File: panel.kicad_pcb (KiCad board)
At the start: 2 copper layers, 91.2 x 81.5 mm, 212 parts, among them J1 PinSocket_1x04_P2.54mm_Vertic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, U1 AP2112K-3.3

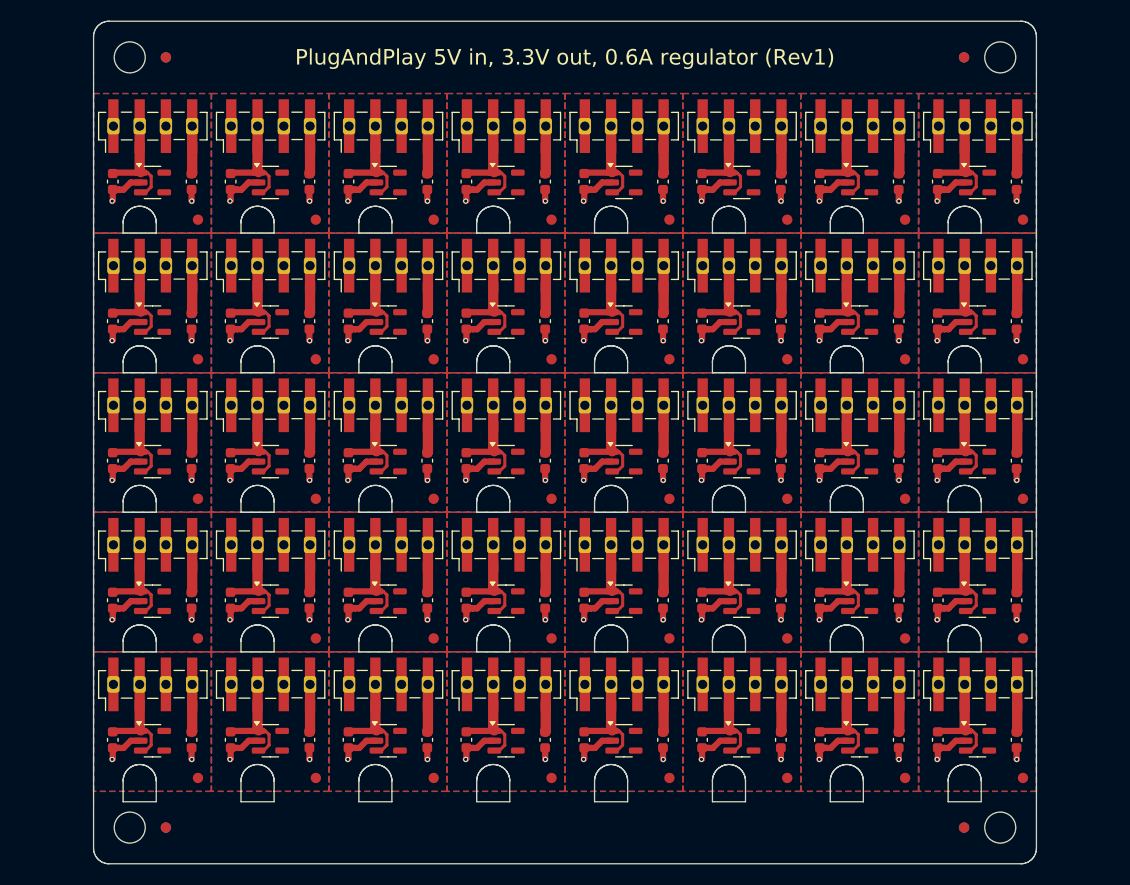
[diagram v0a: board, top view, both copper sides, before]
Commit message: Reduce the screw hole to match M2 screw
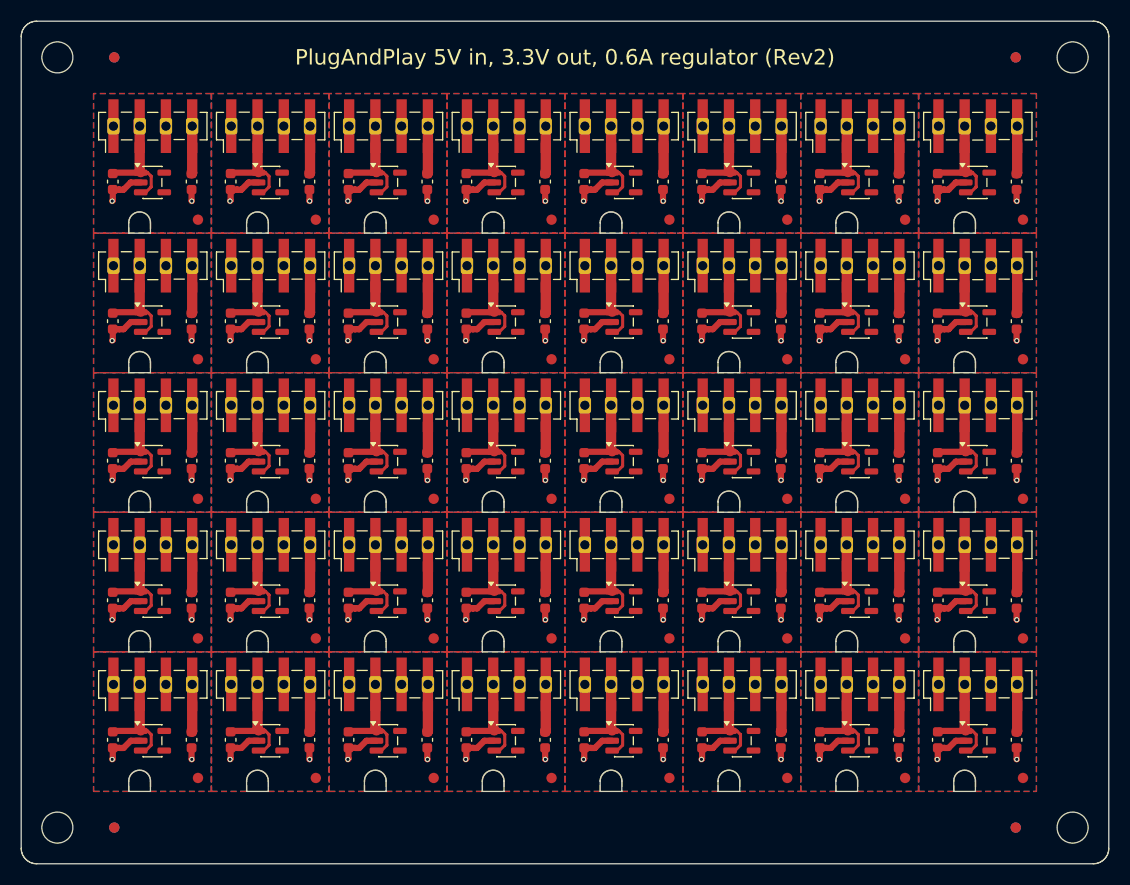
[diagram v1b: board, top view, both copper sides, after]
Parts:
- removed the C1 at (61.3, 76.0)
- removed the C1 at (118.3, 49.0)
- removed the C1 at (141.1, 62.5)
- removed the C1 at (118.3, 35.5)
- removed the C1 at (129.7, 89.5)
- removed the C1 at (84.1, 49.0)
- removed the C1 at (129.7, 49.0)
- removed the C1 at (84.1, 76.0)
- removed the C1 at (84.1, 89.5)
- removed the C1 at (141.1, 49.0)
- removed the C1 at (84.1, 62.5)
- removed the C1 at (95.5, 35.5)
- removed the C1 at (118.3, 62.5)
- removed the C1 at (61.3, 89.5)
- removed the C1 at (72.7, 76.0)
- removed the C1 at (95.5, 76.0)
- removed the C1 at (72.7, 62.5)
- removed the C1 at (118.3, 76.0)
- removed the C1 at (106.9, 49.0)
- removed the C1 at (84.1, 35.5)
- removed the C1 at (106.9, 76.0)
- removed the C1 at (129.7, 76.0)
- removed the C1 at (106.9, 62.5)
- removed the C1 at (72.7, 35.5)
- removed the C1 at (129.7, 62.5)
- removed the C1 at (61.3, 49.0)
- removed the C1 at (118.3, 89.5)
- removed the C1 at (95.5, 62.5)
- removed the C1 at (141.1, 89.5)
- removed the C1 at (72.7, 89.5)
- removed the C1 at (61.3, 35.5)
- removed the C1 at (141.1, 35.5)
- removed the C1 at (61.3, 62.5)
- removed the C1 at (95.5, 49.0)
- removed the C1 at (141.1, 76.0)
- removed the C1 at (129.7, 35.5)
- removed the C1 at (72.7, 49.0)
- removed the C1 at (106.9, 89.5)
- removed the C1 at (106.9, 35.5)
- removed the C1 at (95.5, 89.5)
- removed the C2 at (125.9, 35.5)
- removed the C2 at (137.3, 76.0)
- removed the C2 at (91.7, 35.5)
- removed the C2 at (80.3, 89.5)
- removed the C2 at (68.9, 35.5)
- removed the C2 at (137.3, 62.5)
- removed the C2 at (91.7, 49.0)
- removed the C2 at (114.5, 76.0)
- removed the C2 at (114.5, 89.5)
- removed the C2 at (125.9, 62.5)
- removed the C2 at (103.1, 89.5)
- removed the C2 at (125.9, 49.0)
- removed the C2 at (137.3, 35.5)
- removed the C2 at (68.9, 62.5)
- removed the C2 at (148.7, 49.0)
- removed the C2 at (91.7, 76.0)
- removed the C2 at (137.3, 89.5)
- removed the C2 at (68.9, 49.0)
- removed the C2 at (125.9, 76.0)
- removed the C2 at (68.9, 76.0)
- removed the C2 at (148.7, 35.5)
- removed the C2 at (68.9, 89.5)
- removed the C2 at (80.3, 49.0)
- removed the C2 at (103.1, 49.0)
- removed the C2 at (137.3, 49.0)
- removed the C2 at (148.7, 89.5)
- removed the C2 at (80.3, 62.5)
- removed the C2 at (91.7, 62.5)
- removed the C2 at (103.1, 76.0)
- removed the C2 at (114.5, 49.0)
- removed the C2 at (114.5, 35.5)
- removed the C2 at (103.1, 62.5)
- removed the C2 at (148.7, 62.5)
- removed the C2 at (80.3, 35.5)
- removed the C2 at (114.5, 62.5)
- removed the C2 at (91.7, 89.5)
- removed the C2 at (125.9, 89.5)
- removed the C2 at (148.7, 76.0)
- removed the C2 at (103.1, 35.5)
- removed the C2 at (80.3, 76.0)
- removed the J1 at (133.5, 84.1)
- removed the J1 at (133.5, 57.1)
- removed the J1 at (87.9, 30.1)
- removed the J1 at (99.3, 43.6)
- removed the J1 at (133.5, 70.6)
- removed the J1 at (87.9, 43.6)
- removed the J1 at (76.5, 30.1)
- removed the J1 at (133.5, 30.1)
- removed the J1 at (76.5, 57.1)
- removed the J1 at (87.9, 84.1)
- removed the J1 at (87.9, 57.1)
- removed the J1 at (122.1, 70.6)
- removed the J1 at (122.1, 57.1)
- removed the J1 at (144.9, 57.1)
- removed the J1 at (65.1, 84.1)
- removed the J1 at (133.5, 43.6)
- removed the J1 at (144.9, 43.6)
- removed the J1 at (110.7, 30.1)
- removed the J1 at (144.9, 30.1)
- removed the J1 at (65.1, 43.6)
- removed the J1 at (122.1, 84.1)
- removed the J1 at (122.1, 43.6)
- removed the J1 at (110.7, 70.6)
- removed the J1 at (87.9, 70.6)
- removed the J1 at (110.7, 57.1)
- removed the J1 at (65.1, 30.1)
- removed the J1 at (122.1, 30.1)
- removed the J1 at (99.3, 57.1)
- removed the J1 at (110.7, 84.1)
- removed the J1 at (65.1, 70.6)
- removed the J1 at (99.3, 30.1)
- removed the J1 at (76.5, 43.6)
- removed the J1 at (65.1, 57.1)
- removed the J1 at (99.3, 84.1)
- removed the J1 at (110.7, 43.6)
- removed the J1 at (76.5, 84.1)
- removed the J1 at (99.3, 70.6)
- removed the J1 at (144.9, 70.6)
- removed the J1 at (76.5, 70.6)
- removed the J1 at (144.9, 84.1)
- removed the REF** at (69.5, 52.7)
- removed the REF** at (69.5, 66.2)
- removed the REF** at (126.5, 52.7)
- removed the REF** at (69.5, 39.2)
- removed the REF** at (149.3, 66.2)
- removed the REF** at (80.9, 79.7)
- removed the REF** at (137.9, 66.2)
- removed the REF** at (115.1, 79.7)
- removed the REF** at (137.9, 52.7)
- removed the REF** at (149.3, 39.2)
- removed the REF** at (92.3, 52.7)
- removed the REF** at (137.9, 93.2)
- removed the REF** at (115.1, 39.2)
- removed the REF** at (115.1, 66.2)
- removed the REF** at (92.3, 39.2)
- removed the REF** at (126.5, 79.7)
- removed the REF** at (80.9, 93.2)
- removed the REF** at (69.5, 93.2)
- removed the REF** at (80.9, 66.2)
- removed the REF** at (92.3, 66.2)
- removed the REF** at (149.3, 52.7)
- removed the REF** at (149.3, 79.7)
- removed the REF** at (115.1, 52.7)
- removed the REF** at (115.1, 93.2)
- removed the REF** at (103.7, 52.7)
- removed the REF** at (103.7, 39.2)
- removed the REF** at (137.9, 39.2)
- removed the REF** at (126.5, 93.2)
- removed the REF** at (137.9, 79.7)
- removed the REF** at (92.3, 93.2)
- removed the REF** at (103.7, 66.2)
- removed the REF** at (126.5, 39.2)
- removed the REF** at (92.3, 79.7)
- removed the REF** at (69.5, 79.7)
- removed the REF** at (126.5, 66.2)
- removed the REF** at (149.3, 93.2)
- removed the REF** at (103.7, 79.7)
- removed the REF** at (80.9, 39.2)
- removed the REF** at (80.9, 52.7)
- removed the REF** at (103.7, 93.2)
- removed the U1 at (87.9, 35.6)
- removed the U1 at (65.1, 76.1)
- removed the U1 at (99.3, 89.6)
- removed the U1 at (144.9, 49.1)
- removed the U1 at (133.5, 76.1)
- removed the U1 at (99.3, 49.1)
- removed the U1 at (110.7, 35.6)
- removed the U1 at (122.1, 35.6)
- removed the U1 at (110.7, 89.6)
- removed the U1 at (76.5, 62.6)
- removed the U1 at (87.9, 49.1)
- removed the U1 at (144.9, 35.6)
- removed the U1 at (133.5, 62.6)
- removed the U1 at (110.7, 76.1)
- removed the U1 at (76.5, 35.6)
- removed the U1 at (122.1, 49.1)
- removed the U1 at (133.5, 49.1)
- removed the U1 at (144.9, 89.6)
- removed the U1 at (99.3, 35.6)
- removed the U1 at (76.5, 76.1)
- removed the U1 at (65.1, 89.6)
- removed the U1 at (76.5, 49.1)
- removed the U1 at (65.1, 62.6)
- removed the U1 at (122.1, 76.1)
- removed the U1 at (65.1, 49.1)
- removed the U1 at (65.1, 35.6)
- removed the U1 at (144.9, 76.1)
- removed the U1 at (122.1, 62.6)
- removed the U1 at (99.3, 76.1)
- removed the U1 at (110.7, 49.1)
- removed the U1 at (122.1, 89.6)
- removed the U1 at (87.9, 62.6)
- removed the U1 at (133.5, 89.6)
- removed the U1 at (87.9, 76.1)
- removed the U1 at (110.7, 62.6)
- removed the U1 at (76.5, 89.6)
- removed the U1 at (133.5, 35.6)
- removed the U1 at (99.3, 62.6)
- removed the U1 at (87.9, 89.6)
- removed the U1 at (144.9, 62.6)
- added C1: 1uF, Capacitor_SMD:C_0603_1608Metric, F.Cu at (118.3, 49.0)
- added C1: 1uF, Capacitor_SMD:C_0603_1608Metric, F.Cu at (106.9, 76.0)
- added C1: 1uF, Capacitor_SMD:C_0603_1608Metric, F.Cu at (95.5, 62.5)
- added C1: 1uF, Capacitor_SMD:C_0603_1608Metric, F.Cu at (129.7, 49.0)
- added C1: 1uF, Capacitor_SMD:C_0603_1608Metric, F.Cu at (129.7, 76.0)
- added C1: 1uF, Capacitor_SMD:C_0603_1608Metric, F.Cu at (118.3, 89.5)
- added C1: 1uF, Capacitor_SMD:C_0603_1608Metric, F.Cu at (141.1, 35.5)
- added C1: 1uF, Capacitor_SMD:C_0603_1608Metric, F.Cu at (72.7, 49.0)
- added C1: 1uF, Capacitor_SMD:C_0603_1608Metric, F.Cu at (84.1, 35.5)
- added C1: 1uF, Capacitor_SMD:C_0603_1608Metric, F.Cu at (95.5, 35.5)
- added C1: 1uF, Capacitor_SMD:C_0603_1608Metric, F.Cu at (129.7, 89.5)
- added C1: 1uF, Capacitor_SMD:C_0603_1608Metric, F.Cu at (84.1, 62.5)
- added C1: 1uF, Capacitor_SMD:C_0603_1608Metric, F.Cu at (72.7, 89.5)
- added C1: 1uF, Capacitor_SMD:C_0603_1608Metric, F.Cu at (95.5, 49.0)
- added C1: 1uF, Capacitor_SMD:C_0603_1608Metric, F.Cu at (141.1, 76.0)
- added C1: 1uF, Capacitor_SMD:C_0603_1608Metric, F.Cu at (141.1, 89.5)
- added C1: 1uF, Capacitor_SMD:C_0603_1608Metric, F.Cu at (106.9, 49.0)
- added C1: 1uF, Capacitor_SMD:C_0603_1608Metric, F.Cu at (129.7, 35.5)
- added C1: 1uF, Capacitor_SMD:C_0603_1608Metric, F.Cu at (95.5, 89.5)
- added C1: 1uF, Capacitor_SMD:C_0603_1608Metric, F.Cu at (84.1, 76.0)
- added C1: 1uF, Capacitor_SMD:C_0603_1608Metric, F.Cu at (118.3, 62.5)
- added C1: 1uF, Capacitor_SMD:C_0603_1608Metric, F.Cu at (84.1, 49.0)
- added C1: 1uF, Capacitor_SMD:C_0603_1608Metric, F.Cu at (141.1, 49.0)
- added C1: 1uF, Capacitor_SMD:C_0603_1608Metric, F.Cu at (61.3, 49.0)
- added C1: 1uF, Capacitor_SMD:C_0603_1608Metric, F.Cu at (141.1, 62.5)
- added C1: 1uF, Capacitor_SMD:C_0603_1608Metric, F.Cu at (84.1, 89.5)
- added C1: 1uF, Capacitor_SMD:C_0603_1608Metric, F.Cu at (72.7, 35.5)
- added C1: 1uF, Capacitor_SMD:C_0603_1608Metric, F.Cu at (95.5, 76.0)
- added C1: 1uF, Capacitor_SMD:C_0603_1608Metric, F.Cu at (106.9, 89.5)
- added C1: 1uF, Capacitor_SMD:C_0603_1608Metric, F.Cu at (72.7, 62.5)
- added C1: 1uF, Capacitor_SMD:C_0603_1608Metric, F.Cu at (72.7, 76.0)
- added C1: 1uF, Capacitor_SMD:C_0603_1608Metric, F.Cu at (61.3, 35.5)
- added C1: 1uF, Capacitor_SMD:C_0603_1608Metric, F.Cu at (129.7, 62.5)
- added C1: 1uF, Capacitor_SMD:C_0603_1608Metric, F.Cu at (61.3, 62.5)
- added C1: 1uF, Capacitor_SMD:C_0603_1608Metric, F.Cu at (118.3, 76.0)
- added C1: 1uF, Capacitor_SMD:C_0603_1608Metric, F.Cu at (61.3, 89.5)
- added C1: 1uF, Capacitor_SMD:C_0603_1608Metric, F.Cu at (61.3, 76.0)
- added C1: 1uF, Capacitor_SMD:C_0603_1608Metric, F.Cu at (106.9, 62.5)
- added C1: 1uF, Capacitor_SMD:C_0603_1608Metric, F.Cu at (106.9, 35.5)
- added C1: 1uF, Capacitor_SMD:C_0603_1608Metric, F.Cu at (118.3, 35.5)
- added C2: 1uF, Capacitor_SMD:C_0603_1608Metric, F.Cu at (91.7, 76.0)
- added C2: 1uF, Capacitor_SMD:C_0603_1608Metric, F.Cu at (148.7, 35.5)
- added C2: 1uF, Capacitor_SMD:C_0603_1608Metric, F.Cu at (137.3, 89.5)
- added C2: 1uF, Capacitor_SMD:C_0603_1608Metric, F.Cu at (91.7, 89.5)
- added C2: 1uF, Capacitor_SMD:C_0603_1608Metric, F.Cu at (103.1, 89.5)
- added C2: 1uF, Capacitor_SMD:C_0603_1608Metric, F.Cu at (80.3, 35.5)
- added C2: 1uF, Capacitor_SMD:C_0603_1608Metric, F.Cu at (148.7, 89.5)
- added C2: 1uF, Capacitor_SMD:C_0603_1608Metric, F.Cu at (80.3, 62.5)
- added C2: 1uF, Capacitor_SMD:C_0603_1608Metric, F.Cu at (125.9, 89.5)
- added C2: 1uF, Capacitor_SMD:C_0603_1608Metric, F.Cu at (103.1, 49.0)
- added C2: 1uF, Capacitor_SMD:C_0603_1608Metric, F.Cu at (68.9, 49.0)
- added C2: 1uF, Capacitor_SMD:C_0603_1608Metric, F.Cu at (91.7, 49.0)
- added C2: 1uF, Capacitor_SMD:C_0603_1608Metric, F.Cu at (148.7, 76.0)
- added C2: 1uF, Capacitor_SMD:C_0603_1608Metric, F.Cu at (103.1, 76.0)
- added C2: 1uF, Capacitor_SMD:C_0603_1608Metric, F.Cu at (148.7, 62.5)
- added C2: 1uF, Capacitor_SMD:C_0603_1608Metric, F.Cu at (137.3, 62.5)
- added C2: 1uF, Capacitor_SMD:C_0603_1608Metric, F.Cu at (91.7, 35.5)
- added C2: 1uF, Capacitor_SMD:C_0603_1608Metric, F.Cu at (148.7, 49.0)
- added C2: 1uF, Capacitor_SMD:C_0603_1608Metric, F.Cu at (114.5, 89.5)
- added C2: 1uF, Capacitor_SMD:C_0603_1608Metric, F.Cu at (114.5, 49.0)
- added C2: 1uF, Capacitor_SMD:C_0603_1608Metric, F.Cu at (103.1, 35.5)
- added C2: 1uF, Capacitor_SMD:C_0603_1608Metric, F.Cu at (68.9, 76.0)
- added C2: 1uF, Capacitor_SMD:C_0603_1608Metric, F.Cu at (68.9, 35.5)
- added C2: 1uF, Capacitor_SMD:C_0603_1608Metric, F.Cu at (114.5, 35.5)
- added C2: 1uF, Capacitor_SMD:C_0603_1608Metric, F.Cu at (114.5, 62.5)
- added C2: 1uF, Capacitor_SMD:C_0603_1608Metric, F.Cu at (80.3, 89.5)
- added C2: 1uF, Capacitor_SMD:C_0603_1608Metric, F.Cu at (125.9, 49.0)
- added C2: 1uF, Capacitor_SMD:C_0603_1608Metric, F.Cu at (68.9, 89.5)
- added C2: 1uF, Capacitor_SMD:C_0603_1608Metric, F.Cu at (137.3, 35.5)
- added C2: 1uF, Capacitor_SMD:C_0603_1608Metric, F.Cu at (103.1, 62.5)
- added C2: 1uF, Capacitor_SMD:C_0603_1608Metric, F.Cu at (125.9, 76.0)
- added C2: 1uF, Capacitor_SMD:C_0603_1608Metric, F.Cu at (137.3, 76.0)
- added C2: 1uF, Capacitor_SMD:C_0603_1608Metric, F.Cu at (125.9, 62.5)
- added C2: 1uF, Capacitor_SMD:C_0603_1608Metric, F.Cu at (125.9, 35.5)
- added C2: 1uF, Capacitor_SMD:C_0603_1608Metric, F.Cu at (80.3, 49.0)
- added C2: 1uF, Capacitor_SMD:C_0603_1608Metric, F.Cu at (137.3, 49.0)
- added C2: 1uF, Capacitor_SMD:C_0603_1608Metric, F.Cu at (114.5, 76.0)
- added C2: 1uF, Capacitor_SMD:C_0603_1608Metric, F.Cu at (80.3, 76.0)
- added C2: 1uF, Capacitor_SMD:C_0603_1608Metric, F.Cu at (68.9, 62.5)
- added C2: 1uF, Capacitor_SMD:C_0603_1608Metric, F.Cu at (91.7, 62.5)
- added J1: PinSocket_1x04_P2.54mm_Vertical_SMD_Pin1Left, Library:PinSocket_1x04_P2.54mm_Vertical_SMD_Pin1Left, F.Cu at (87.9, 70.7)
- added J1: PinSocket_1x04_P2.54mm_Vertical_SMD_Pin1Left, Library:PinSocket_1x04_P2.54mm_Vertical_SMD_Pin1Left, F.Cu at (122.1, 43.6)
- added J1: PinSocket_1x04_P2.54mm_Vertical_SMD_Pin1Left, Library:PinSocket_1x04_P2.54mm_Vertical_SMD_Pin1Left, F.Cu at (133.5, 43.6)
- added J1: PinSocket_1x04_P2.54mm_Vertical_SMD_Pin1Left, Library:PinSocket_1x04_P2.54mm_Vertical_SMD_Pin1Left, F.Cu at (122.1, 57.1)
- added J1: PinSocket_1x04_P2.54mm_Vertical_SMD_Pin1Left, Library:PinSocket_1x04_P2.54mm_Vertical_SMD_Pin1Left, F.Cu at (122.1, 30.1)
- added J1: PinSocket_1x04_P2.54mm_Vertical_SMD_Pin1Left, Library:PinSocket_1x04_P2.54mm_Vertical_SMD_Pin1Left, F.Cu at (76.5, 30.1)
- added J1: PinSocket_1x04_P2.54mm_Vertical_SMD_Pin1Left, Library:PinSocket_1x04_P2.54mm_Vertical_SMD_Pin1Left, F.Cu at (99.3, 57.1)
- added J1: PinSocket_1x04_P2.54mm_Vertical_SMD_Pin1Left, Library:PinSocket_1x04_P2.54mm_Vertical_SMD_Pin1Left, F.Cu at (133.5, 57.1)
- added J1: PinSocket_1x04_P2.54mm_Vertical_SMD_Pin1Left, Library:PinSocket_1x04_P2.54mm_Vertical_SMD_Pin1Left, F.Cu at (99.3, 43.6)
- added J1: PinSocket_1x04_P2.54mm_Vertical_SMD_Pin1Left, Library:PinSocket_1x04_P2.54mm_Vertical_SMD_Pin1Left, F.Cu at (144.9, 57.1)
- added J1: PinSocket_1x04_P2.54mm_Vertical_SMD_Pin1Left, Library:PinSocket_1x04_P2.54mm_Vertical_SMD_Pin1Left, F.Cu at (65.1, 57.1)
- added J1: PinSocket_1x04_P2.54mm_Vertical_SMD_Pin1Left, Library:PinSocket_1x04_P2.54mm_Vertical_SMD_Pin1Left, F.Cu at (144.9, 30.1)
- added J1: PinSocket_1x04_P2.54mm_Vertical_SMD_Pin1Left, Library:PinSocket_1x04_P2.54mm_Vertical_SMD_Pin1Left, F.Cu at (144.9, 43.6)
- added J1: PinSocket_1x04_P2.54mm_Vertical_SMD_Pin1Left, Library:PinSocket_1x04_P2.54mm_Vertical_SMD_Pin1Left, F.Cu at (133.5, 84.2)
- added J1: PinSocket_1x04_P2.54mm_Vertical_SMD_Pin1Left, Library:PinSocket_1x04_P2.54mm_Vertical_SMD_Pin1Left, F.Cu at (76.5, 43.6)
- added J1: PinSocket_1x04_P2.54mm_Vertical_SMD_Pin1Left, Library:PinSocket_1x04_P2.54mm_Vertical_SMD_Pin1Left, F.Cu at (110.7, 70.7)
- added J1: PinSocket_1x04_P2.54mm_Vertical_SMD_Pin1Left, Library:PinSocket_1x04_P2.54mm_Vertical_SMD_Pin1Left, F.Cu at (87.9, 57.1)
- added J1: PinSocket_1x04_P2.54mm_Vertical_SMD_Pin1Left, Library:PinSocket_1x04_P2.54mm_Vertical_SMD_Pin1Left, F.Cu at (76.5, 70.7)
- added J1: PinSocket_1x04_P2.54mm_Vertical_SMD_Pin1Left, Library:PinSocket_1x04_P2.54mm_Vertical_SMD_Pin1Left, F.Cu at (110.7, 30.1)
- added J1: PinSocket_1x04_P2.54mm_Vertical_SMD_Pin1Left, Library:PinSocket_1x04_P2.54mm_Vertical_SMD_Pin1Left, F.Cu at (133.5, 30.1)
- added J1: PinSocket_1x04_P2.54mm_Vertical_SMD_Pin1Left, Library:PinSocket_1x04_P2.54mm_Vertical_SMD_Pin1Left, F.Cu at (99.3, 30.1)
- added J1: PinSocket_1x04_P2.54mm_Vertical_SMD_Pin1Left, Library:PinSocket_1x04_P2.54mm_Vertical_SMD_Pin1Left, F.Cu at (87.9, 84.2)
- added J1: PinSocket_1x04_P2.54mm_Vertical_SMD_Pin1Left, Library:PinSocket_1x04_P2.54mm_Vertical_SMD_Pin1Left, F.Cu at (65.1, 43.6)
- added J1: PinSocket_1x04_P2.54mm_Vertical_SMD_Pin1Left, Library:PinSocket_1x04_P2.54mm_Vertical_SMD_Pin1Left, F.Cu at (122.1, 84.2)
- added J1: PinSocket_1x04_P2.54mm_Vertical_SMD_Pin1Left, Library:PinSocket_1x04_P2.54mm_Vertical_SMD_Pin1Left, F.Cu at (144.9, 84.2)
- added J1: PinSocket_1x04_P2.54mm_Vertical_SMD_Pin1Left, Library:PinSocket_1x04_P2.54mm_Vertical_SMD_Pin1Left, F.Cu at (110.7, 43.6)
- added J1: PinSocket_1x04_P2.54mm_Vertical_SMD_Pin1Left, Library:PinSocket_1x04_P2.54mm_Vertical_SMD_Pin1Left, F.Cu at (122.1, 70.7)
- added J1: PinSocket_1x04_P2.54mm_Vertical_SMD_Pin1Left, Library:PinSocket_1x04_P2.54mm_Vertical_SMD_Pin1Left, F.Cu at (144.9, 70.7)
- added J1: PinSocket_1x04_P2.54mm_Vertical_SMD_Pin1Left, Library:PinSocket_1x04_P2.54mm_Vertical_SMD_Pin1Left, F.Cu at (76.5, 57.1)
- added J1: PinSocket_1x04_P2.54mm_Vertical_SMD_Pin1Left, Library:PinSocket_1x04_P2.54mm_Vertical_SMD_Pin1Left, F.Cu at (65.1, 30.1)
- added J1: PinSocket_1x04_P2.54mm_Vertical_SMD_Pin1Left, Library:PinSocket_1x04_P2.54mm_Vertical_SMD_Pin1Left, F.Cu at (65.1, 84.2)
- added J1: PinSocket_1x04_P2.54mm_Vertical_SMD_Pin1Left, Library:PinSocket_1x04_P2.54mm_Vertical_SMD_Pin1Left, F.Cu at (65.1, 70.7)
- added J1: PinSocket_1x04_P2.54mm_Vertical_SMD_Pin1Left, Library:PinSocket_1x04_P2.54mm_Vertical_SMD_Pin1Left, F.Cu at (133.5, 70.7)
- added J1: PinSocket_1x04_P2.54mm_Vertical_SMD_Pin1Left, Library:PinSocket_1x04_P2.54mm_Vertical_SMD_Pin1Left, F.Cu at (110.7, 57.1)
- added J1: PinSocket_1x04_P2.54mm_Vertical_SMD_Pin1Left, Library:PinSocket_1x04_P2.54mm_Vertical_SMD_Pin1Left, F.Cu at (87.9, 43.6)
- added J1: PinSocket_1x04_P2.54mm_Vertical_SMD_Pin1Left, Library:PinSocket_1x04_P2.54mm_Vertical_SMD_Pin1Left, F.Cu at (76.5, 84.2)
- added J1: PinSocket_1x04_P2.54mm_Vertical_SMD_Pin1Left, Library:PinSocket_1x04_P2.54mm_Vertical_SMD_Pin1Left, F.Cu at (87.9, 30.1)
- added J1: PinSocket_1x04_P2.54mm_Vertical_SMD_Pin1Left, Library:PinSocket_1x04_P2.54mm_Vertical_SMD_Pin1Left, F.Cu at (99.3, 84.2)
- added J1: PinSocket_1x04_P2.54mm_Vertical_SMD_Pin1Left, Library:PinSocket_1x04_P2.54mm_Vertical_SMD_Pin1Left, F.Cu at (99.3, 70.7)
- added J1: PinSocket_1x04_P2.54mm_Vertical_SMD_Pin1Left, Library:PinSocket_1x04_P2.54mm_Vertical_SMD_Pin1Left, F.Cu at (110.7, 84.2)
- added REF**: Fiducial_1mm_Mask2mm, Fiducial:Fiducial_1mm_Mask2mm, F.Cu at (103.7, 66.2)
- added REF**: Fiducial_1mm_Mask2mm, Fiducial:Fiducial_1mm_Mask2mm, F.Cu at (115.1, 39.2)
- added REF**: Fiducial_1mm_Mask2mm, Fiducial:Fiducial_1mm_Mask2mm, F.Cu at (69.5, 39.2)
- added REF**: Fiducial_1mm_Mask2mm, Fiducial:Fiducial_1mm_Mask2mm, F.Cu at (69.5, 52.7)
- added REF**: Fiducial_1mm_Mask2mm, Fiducial:Fiducial_1mm_Mask2mm, F.Cu at (137.9, 79.7)
- added REF**: Fiducial_1mm_Mask2mm, Fiducial:Fiducial_1mm_Mask2mm, F.Cu at (69.5, 93.2)
- added REF**: Fiducial_1mm_Mask2mm, Fiducial:Fiducial_1mm_Mask2mm, F.Cu at (103.7, 79.7)
- added REF**: Fiducial_1mm_Mask2mm, Fiducial:Fiducial_1mm_Mask2mm, F.Cu at (126.5, 79.7)
- added REF**: Fiducial_1mm_Mask2mm, Fiducial:Fiducial_1mm_Mask2mm, F.Cu at (115.1, 52.7)
- added REF**: Fiducial_1mm_Mask2mm, Fiducial:Fiducial_1mm_Mask2mm, F.Cu at (115.1, 79.7)
- added REF**: Fiducial_1mm_Mask2mm, Fiducial:Fiducial_1mm_Mask2mm, F.Cu at (69.5, 79.7)
- added REF**: Fiducial_1mm_Mask2mm, Fiducial:Fiducial_1mm_Mask2mm, F.Cu at (80.9, 39.2)
- added REF**: Fiducial_1mm_Mask2mm, Fiducial:Fiducial_1mm_Mask2mm, F.Cu at (103.7, 93.2)
- added REF**: Fiducial_1mm_Mask2mm, Fiducial:Fiducial_1mm_Mask2mm, F.Cu at (92.3, 66.2)
- added REF**: Fiducial_1mm_Mask2mm, Fiducial:Fiducial_1mm_Mask2mm, F.Cu at (103.7, 39.2)
- added REF**: Fiducial_1mm_Mask2mm, Fiducial:Fiducial_1mm_Mask2mm, F.Cu at (69.5, 66.2)
- added REF**: Fiducial_1mm_Mask2mm, Fiducial:Fiducial_1mm_Mask2mm, F.Cu at (126.5, 66.2)
- added REF**: Fiducial_1mm_Mask2mm, Fiducial:Fiducial_1mm_Mask2mm, F.Cu at (149.3, 66.2)
- added REF**: Fiducial_1mm_Mask2mm, Fiducial:Fiducial_1mm_Mask2mm, F.Cu at (92.3, 52.7)
- added REF**: Fiducial_1mm_Mask2mm, Fiducial:Fiducial_1mm_Mask2mm, F.Cu at (126.5, 93.2)
- added REF**: Fiducial_1mm_Mask2mm, Fiducial:Fiducial_1mm_Mask2mm, F.Cu at (137.9, 52.7)
- added REF**: Fiducial_1mm_Mask2mm, Fiducial:Fiducial_1mm_Mask2mm, F.Cu at (103.7, 52.7)
- added REF**: Fiducial_1mm_Mask2mm, Fiducial:Fiducial_1mm_Mask2mm, F.Cu at (80.9, 79.7)
- added REF**: Fiducial_1mm_Mask2mm, Fiducial:Fiducial_1mm_Mask2mm, F.Cu at (126.5, 39.2)
- added REF**: Fiducial_1mm_Mask2mm, Fiducial:Fiducial_1mm_Mask2mm, F.Cu at (92.3, 93.2)
- added REF**: Fiducial_1mm_Mask2mm, Fiducial:Fiducial_1mm_Mask2mm, F.Cu at (149.3, 39.2)
- added REF**: Fiducial_1mm_Mask2mm, Fiducial:Fiducial_1mm_Mask2mm, F.Cu at (115.1, 66.2)
- added REF**: Fiducial_1mm_Mask2mm, Fiducial:Fiducial_1mm_Mask2mm, F.Cu at (80.9, 66.2)
- added REF**: Fiducial_1mm_Mask2mm, Fiducial:Fiducial_1mm_Mask2mm, F.Cu at (115.1, 93.2)
- added REF**: Fiducial_1mm_Mask2mm, Fiducial:Fiducial_1mm_Mask2mm, F.Cu at (149.3, 79.7)
- added REF**: Fiducial_1mm_Mask2mm, Fiducial:Fiducial_1mm_Mask2mm, F.Cu at (126.5, 52.7)
- added REF**: Fiducial_1mm_Mask2mm, Fiducial:Fiducial_1mm_Mask2mm, F.Cu at (80.9, 93.2)
- added REF**: Fiducial_1mm_Mask2mm, Fiducial:Fiducial_1mm_Mask2mm, F.Cu at (137.9, 39.2)
- added REF**: Fiducial_1mm_Mask2mm, Fiducial:Fiducial_1mm_Mask2mm, F.Cu at (92.3, 39.2)
- added REF**: Fiducial_1mm_Mask2mm, Fiducial:Fiducial_1mm_Mask2mm, F.Cu at (149.3, 52.7)
- added REF**: Fiducial_1mm_Mask2mm, Fiducial:Fiducial_1mm_Mask2mm, F.Cu at (92.3, 79.7)
- added REF**: Fiducial_1mm_Mask2mm, Fiducial:Fiducial_1mm_Mask2mm, F.Cu at (137.9, 66.2)
- added REF**: Fiducial_1mm_Mask2mm, Fiducial:Fiducial_1mm_Mask2mm, F.Cu at (80.9, 52.7)
- added REF**: Fiducial_1mm_Mask2mm, Fiducial:Fiducial_1mm_Mask2mm, F.Cu at (149.3, 93.2)
- added REF**: Fiducial_1mm_Mask2mm, Fiducial:Fiducial_1mm_Mask2mm, F.Cu at (137.9, 93.2)
- added U1: AP2112K-3.3, Package_TO_SOT_SMD:SOT-23-5, F.Cu at (87.9, 35.6)
- added U1: AP2112K-3.3, Package_TO_SOT_SMD:SOT-23-5, F.Cu at (87.9, 89.6)
- added U1: AP2112K-3.3, Package_TO_SOT_SMD:SOT-23-5, F.Cu at (87.9, 49.1)
- added U1: AP2112K-3.3, Package_TO_SOT_SMD:SOT-23-5, F.Cu at (65.1, 35.6)
- added U1: AP2112K-3.3, Package_TO_SOT_SMD:SOT-23-5, F.Cu at (122.1, 35.6)
- added U1: AP2112K-3.3, Package_TO_SOT_SMD:SOT-23-5, F.Cu at (99.3, 35.6)
- added U1: AP2112K-3.3, Package_TO_SOT_SMD:SOT-23-5, F.Cu at (76.5, 89.6)
- added U1: AP2112K-3.3, Package_TO_SOT_SMD:SOT-23-5, F.Cu at (144.9, 62.6)
- added U1: AP2112K-3.3, Package_TO_SOT_SMD:SOT-23-5, F.Cu at (110.7, 62.6)
- added U1: AP2112K-3.3, Package_TO_SOT_SMD:SOT-23-5, F.Cu at (133.5, 49.1)
- added U1: AP2112K-3.3, Package_TO_SOT_SMD:SOT-23-5, F.Cu at (99.3, 76.1)
- added U1: AP2112K-3.3, Package_TO_SOT_SMD:SOT-23-5, F.Cu at (122.1, 89.6)
- added U1: AP2112K-3.3, Package_TO_SOT_SMD:SOT-23-5, F.Cu at (65.1, 76.1)
- added U1: AP2112K-3.3, Package_TO_SOT_SMD:SOT-23-5, F.Cu at (87.9, 62.6)
- added U1: AP2112K-3.3, Package_TO_SOT_SMD:SOT-23-5, F.Cu at (65.1, 62.6)
- added U1: AP2112K-3.3, Package_TO_SOT_SMD:SOT-23-5, F.Cu at (110.7, 35.6)
- added U1: AP2112K-3.3, Package_TO_SOT_SMD:SOT-23-5, F.Cu at (133.5, 76.1)
- added U1: AP2112K-3.3, Package_TO_SOT_SMD:SOT-23-5, F.Cu at (65.1, 89.6)
- added U1: AP2112K-3.3, Package_TO_SOT_SMD:SOT-23-5, F.Cu at (76.5, 35.6)
- added U1: AP2112K-3.3, Package_TO_SOT_SMD:SOT-23-5, F.Cu at (87.9, 76.1)
- added U1: AP2112K-3.3, Package_TO_SOT_SMD:SOT-23-5, F.Cu at (76.5, 49.1)
- added U1: AP2112K-3.3, Package_TO_SOT_SMD:SOT-23-5, F.Cu at (110.7, 49.1)
- added U1: AP2112K-3.3, Package_TO_SOT_SMD:SOT-23-5, F.Cu at (110.7, 89.6)
- added U1: AP2112K-3.3, Package_TO_SOT_SMD:SOT-23-5, F.Cu at (99.3, 62.6)
- added U1: AP2112K-3.3, Package_TO_SOT_SMD:SOT-23-5, F.Cu at (122.1, 49.1)
- added U1: AP2112K-3.3, Package_TO_SOT_SMD:SOT-23-5, F.Cu at (133.5, 89.6)
- added U1: AP2112K-3.3, Package_TO_SOT_SMD:SOT-23-5, F.Cu at (99.3, 49.1)
- added U1: AP2112K-3.3, Package_TO_SOT_SMD:SOT-23-5, F.Cu at (144.9, 35.6)
- added U1: AP2112K-3.3, Package_TO_SOT_SMD:SOT-23-5, F.Cu at (144.9, 89.6)
- added U1: AP2112K-3.3, Package_TO_SOT_SMD:SOT-23-5, F.Cu at (122.1, 76.1)
- added U1: AP2112K-3.3, Package_TO_SOT_SMD:SOT-23-5, F.Cu at (144.9, 49.1)
- added U1: AP2112K-3.3, Package_TO_SOT_SMD:SOT-23-5, F.Cu at (65.1, 49.1)
- added U1: AP2112K-3.3, Package_TO_SOT_SMD:SOT-23-5, F.Cu at (76.5, 76.1)
- added U1: AP2112K-3.3, Package_TO_SOT_SMD:SOT-23-5, F.Cu at (122.1, 62.6)
- added U1: AP2112K-3.3, Package_TO_SOT_SMD:SOT-23-5, F.Cu at (144.9, 76.1)
- added U1: AP2112K-3.3, Package_TO_SOT_SMD:SOT-23-5, F.Cu at (133.5, 62.6)
- added U1: AP2112K-3.3, Package_TO_SOT_SMD:SOT-23-5, F.Cu at (110.7, 76.1)
- added U1: AP2112K-3.3, Package_TO_SOT_SMD:SOT-23-5, F.Cu at (99.3, 89.6)
- added U1: AP2112K-3.3, Package_TO_SOT_SMD:SOT-23-5, F.Cu at (76.5, 62.6)
- added U1: AP2112K-3.3, Package_TO_SOT_SMD:SOT-23-5, F.Cu at (133.5, 35.6)
- moved KiKit_TO_3 7.00 mm to (55.9, 98.0)
- moved KiKit_TO_4 7.00 mm to (154.1, 98.0)
- moved KiKit_TO_1 7.00 mm to (55.9, 23.5)
- moved KiKit_TO_2 7.00 mm to (154.1, 23.5)
- moved KiKit_FID_B_3 5.00 mm to (61.4, 98.0), turned to 180 degrees
- moved KiKit_FID_T_3 5.00 mm to (61.4, 98.0)
- moved KiKit_FID_B_4 5.00 mm to (148.6, 98.0), turned to 180 degrees
- moved KiKit_FID_T_4 5.00 mm to (148.6, 98.0)
- moved KiKit_FID_B_1 5.00 mm to (61.4, 23.5), turned to 180 degrees
- moved KiKit_FID_T_1 5.00 mm to (61.4, 23.5)
- moved KiKit_FID_B_2 5.00 mm to (148.6, 23.5), turned to 180 degrees
- moved KiKit_FID_T_2 5.00 mm to (148.6, 23.5)
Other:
- board size 91.2 x 81.5 mm -> 105.2 x 81.5 mm
- board text added: "PlugAndPlay 5V in, 3.3V out, 0.6A regulator (Rev2)"
- board text removed: "PlugAndPlay 5V in, 3.3V out, 0.6A regulator (Rev1)"

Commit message: Change connector name from socket to header. Some minor traces changes.
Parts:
- removed the J1 at (87.9, 70.7)
- removed the J1 at (122.1, 43.6)
- removed the J1 at (133.5, 43.6)
- removed the J1 at (122.1, 57.1)
- removed the J1 at (122.1, 30.1)
- removed the J1 at (76.5, 30.1)
- removed the J1 at (99.3, 57.1)
- removed the J1 at (133.5, 57.1)
- removed the J1 at (99.3, 43.6)
- removed the J1 at (144.9, 57.1)
- removed the J1 at (65.1, 57.1)
- removed the J1 at (144.9, 30.1)
- removed the J1 at (144.9, 43.6)
- removed the J1 at (133.5, 84.2)
- removed the J1 at (76.5, 43.6)
- removed the J1 at (110.7, 70.7)
- removed the J1 at (87.9, 57.1)
- removed the J1 at (76.5, 70.7)
- removed the J1 at (110.7, 30.1)
- removed the J1 at (133.5, 30.1)
- removed the J1 at (99.3, 30.1)
- removed the J1 at (87.9, 84.2)
- removed the J1 at (65.1, 43.6)
- removed the J1 at (122.1, 84.2)
- removed the J1 at (144.9, 84.2)
- removed the J1 at (110.7, 43.6)
- removed the J1 at (122.1, 70.7)
- removed the J1 at (144.9, 70.7)
- removed the J1 at (76.5, 57.1)
- removed the J1 at (65.1, 30.1)
- removed the J1 at (65.1, 84.2)
- removed the J1 at (65.1, 70.7)
- removed the J1 at (133.5, 70.7)
- removed the J1 at (110.7, 57.1)
- removed the J1 at (87.9, 43.6)
- removed the J1 at (76.5, 84.2)
- removed the J1 at (87.9, 30.1)
- removed the J1 at (99.3, 84.2)
- removed the J1 at (99.3, 70.7)
- removed the J1 at (110.7, 84.2)
- added J1: PinHeader_1x04_P2.54mm_Vertical_SMD_Pin1Left, PnP_Library:PinSocket_1x04_P2.54mm_Vertical_SMD_Pin1Left, F.Cu at (122.1, 84.2)
- added J1: PinHeader_1x04_P2.54mm_Vertical_SMD_Pin1Left, PnP_Library:PinSocket_1x04_P2.54mm_Vertical_SMD_Pin1Left, F.Cu at (87.9, 43.6)
- added J1: PinHeader_1x04_P2.54mm_Vertical_SMD_Pin1Left, PnP_Library:PinSocket_1x04_P2.54mm_Vertical_SMD_Pin1Left, F.Cu at (110.7, 70.7)
- added J1: PinHeader_1x04_P2.54mm_Vertical_SMD_Pin1Left, PnP_Library:PinSocket_1x04_P2.54mm_Vertical_SMD_Pin1Left, F.Cu at (110.7, 30.1)
- added J1: PinHeader_1x04_P2.54mm_Vertical_SMD_Pin1Left, PnP_Library:PinSocket_1x04_P2.54mm_Vertical_SMD_Pin1Left, F.Cu at (133.5, 57.1)
- added J1: PinHeader_1x04_P2.54mm_Vertical_SMD_Pin1Left, PnP_Library:PinSocket_1x04_P2.54mm_Vertical_SMD_Pin1Left, F.Cu at (65.1, 70.7)
- added J1: PinHeader_1x04_P2.54mm_Vertical_SMD_Pin1Left, PnP_Library:PinSocket_1x04_P2.54mm_Vertical_SMD_Pin1Left, F.Cu at (76.5, 57.1)
- added J1: PinHeader_1x04_P2.54mm_Vertical_SMD_Pin1Left, PnP_Library:PinSocket_1x04_P2.54mm_Vertical_SMD_Pin1Left, F.Cu at (87.9, 30.1)
- added J1: PinHeader_1x04_P2.54mm_Vertical_SMD_Pin1Left, PnP_Library:PinSocket_1x04_P2.54mm_Vertical_SMD_Pin1Left, F.Cu at (133.5, 30.1)
- added J1: PinHeader_1x04_P2.54mm_Vertical_SMD_Pin1Left, PnP_Library:PinSocket_1x04_P2.54mm_Vertical_SMD_Pin1Left, F.Cu at (99.3, 70.7)
- added J1: PinHeader_1x04_P2.54mm_Vertical_SMD_Pin1Left, PnP_Library:PinSocket_1x04_P2.54mm_Vertical_SMD_Pin1Left, F.Cu at (87.9, 70.7)
- added J1: PinHeader_1x04_P2.54mm_Vertical_SMD_Pin1Left, PnP_Library:PinSocket_1x04_P2.54mm_Vertical_SMD_Pin1Left, F.Cu at (122.1, 43.6)
- added J1: PinHeader_1x04_P2.54mm_Vertical_SMD_Pin1Left, PnP_Library:PinSocket_1x04_P2.54mm_Vertical_SMD_Pin1Left, F.Cu at (110.7, 57.1)
- added J1: PinHeader_1x04_P2.54mm_Vertical_SMD_Pin1Left, PnP_Library:PinSocket_1x04_P2.54mm_Vertical_SMD_Pin1Left, F.Cu at (99.3, 30.1)
- added J1: PinHeader_1x04_P2.54mm_Vertical_SMD_Pin1Left, PnP_Library:PinSocket_1x04_P2.54mm_Vertical_SMD_Pin1Left, F.Cu at (87.9, 57.1)
- added J1: PinHeader_1x04_P2.54mm_Vertical_SMD_Pin1Left, PnP_Library:PinSocket_1x04_P2.54mm_Vertical_SMD_Pin1Left, F.Cu at (133.5, 43.6)
- added J1: PinHeader_1x04_P2.54mm_Vertical_SMD_Pin1Left, PnP_Library:PinSocket_1x04_P2.54mm_Vertical_SMD_Pin1Left, F.Cu at (76.5, 84.2)
- added J1: PinHeader_1x04_P2.54mm_Vertical_SMD_Pin1Left, PnP_Library:PinSocket_1x04_P2.54mm_Vertical_SMD_Pin1Left, F.Cu at (99.3, 84.2)
- added J1: PinHeader_1x04_P2.54mm_Vertical_SMD_Pin1Left, PnP_Library:PinSocket_1x04_P2.54mm_Vertical_SMD_Pin1Left, F.Cu at (110.7, 43.6)
- added J1: PinHeader_1x04_P2.54mm_Vertical_SMD_Pin1Left, PnP_Library:PinSocket_1x04_P2.54mm_Vertical_SMD_Pin1Left, F.Cu at (99.3, 43.6)
- added J1: PinHeader_1x04_P2.54mm_Vertical_SMD_Pin1Left, PnP_Library:PinSocket_1x04_P2.54mm_Vertical_SMD_Pin1Left, F.Cu at (133.5, 70.7)
- added J1: PinHeader_1x04_P2.54mm_Vertical_SMD_Pin1Left, PnP_Library:PinSocket_1x04_P2.54mm_Vertical_SMD_Pin1Left, F.Cu at (76.5, 70.7)
- added J1: PinHeader_1x04_P2.54mm_Vertical_SMD_Pin1Left, PnP_Library:PinSocket_1x04_P2.54mm_Vertical_SMD_Pin1Left, F.Cu at (65.1, 57.1)
- added J1: PinHeader_1x04_P2.54mm_Vertical_SMD_Pin1Left, PnP_Library:PinSocket_1x04_P2.54mm_Vertical_SMD_Pin1Left, F.Cu at (144.9, 30.1)
- added J1: PinHeader_1x04_P2.54mm_Vertical_SMD_Pin1Left, PnP_Library:PinSocket_1x04_P2.54mm_Vertical_SMD_Pin1Left, F.Cu at (144.9, 84.2)
- added J1: PinHeader_1x04_P2.54mm_Vertical_SMD_Pin1Left, PnP_Library:PinSocket_1x04_P2.54mm_Vertical_SMD_Pin1Left, F.Cu at (110.7, 84.2)
- added J1: PinHeader_1x04_P2.54mm_Vertical_SMD_Pin1Left, PnP_Library:PinSocket_1x04_P2.54mm_Vertical_SMD_Pin1Left, F.Cu at (87.9, 84.2)
- added J1: PinHeader_1x04_P2.54mm_Vertical_SMD_Pin1Left, PnP_Library:PinSocket_1x04_P2.54mm_Vertical_SMD_Pin1Left, F.Cu at (99.3, 57.1)
- added J1: PinHeader_1x04_P2.54mm_Vertical_SMD_Pin1Left, PnP_Library:PinSocket_1x04_P2.54mm_Vertical_SMD_Pin1Left, F.Cu at (144.9, 70.7)
- added J1: PinHeader_1x04_P2.54mm_Vertical_SMD_Pin1Left, PnP_Library:PinSocket_1x04_P2.54mm_Vertical_SMD_Pin1Left, F.Cu at (122.1, 57.1)
- added J1: PinHeader_1x04_P2.54mm_Vertical_SMD_Pin1Left, PnP_Library:PinSocket_1x04_P2.54mm_Vertical_SMD_Pin1Left, F.Cu at (65.1, 30.1)
- added J1: PinHeader_1x04_P2.54mm_Vertical_SMD_Pin1Left, PnP_Library:PinSocket_1x04_P2.54mm_Vertical_SMD_Pin1Left, F.Cu at (76.5, 43.6)
- added J1: PinHeader_1x04_P2.54mm_Vertical_SMD_Pin1Left, PnP_Library:PinSocket_1x04_P2.54mm_Vertical_SMD_Pin1Left, F.Cu at (144.9, 57.1)
- added J1: PinHeader_1x04_P2.54mm_Vertical_SMD_Pin1Left, PnP_Library:PinSocket_1x04_P2.54mm_Vertical_SMD_Pin1Left, F.Cu at (76.5, 30.1)
- added J1: PinHeader_1x04_P2.54mm_Vertical_SMD_Pin1Left, PnP_Library:PinSocket_1x04_P2.54mm_Vertical_SMD_Pin1Left, F.Cu at (144.9, 43.6)
- added J1: PinHeader_1x04_P2.54mm_Vertical_SMD_Pin1Left, PnP_Library:PinSocket_1x04_P2.54mm_Vertical_SMD_Pin1Left, F.Cu at (122.1, 30.1)
- added J1: PinHeader_1x04_P2.54mm_Vertical_SMD_Pin1Left, PnP_Library:PinSocket_1x04_P2.54mm_Vertical_SMD_Pin1Left, F.Cu at (65.1, 84.2)
- added J1: PinHeader_1x04_P2.54mm_Vertical_SMD_Pin1Left, PnP_Library:PinSocket_1x04_P2.54mm_Vertical_SMD_Pin1Left, F.Cu at (65.1, 43.6)
- added J1: PinHeader_1x04_P2.54mm_Vertical_SMD_Pin1Left, PnP_Library:PinSocket_1x04_P2.54mm_Vertical_SMD_Pin1Left, F.Cu at (122.1, 70.7)
- added J1: PinHeader_1x04_P2.54mm_Vertical_SMD_Pin1Left, PnP_Library:PinSocket_1x04_P2.54mm_Vertical_SMD_Pin1Left, F.Cu at (133.5, 84.2)
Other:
- outline, holes or cut-outs redrawn
